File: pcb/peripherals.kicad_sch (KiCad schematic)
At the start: 32 parts, among them U2 PCA9545APW, U3 AHT20-F, U4 LTR-303ALS-01, U5 SGP40-D-R4

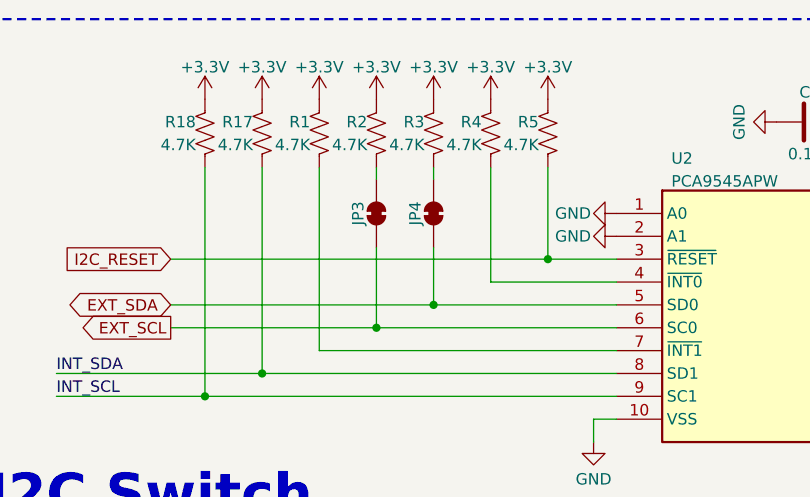
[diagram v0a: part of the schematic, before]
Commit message: Changed I2C to open instead of bridged
Moved I2C jumper to back
Changed to open instead of bridged
Changed Roxy to 5mm on front
Moved silkscreen around.
Updated renders
Removed logos from BOM
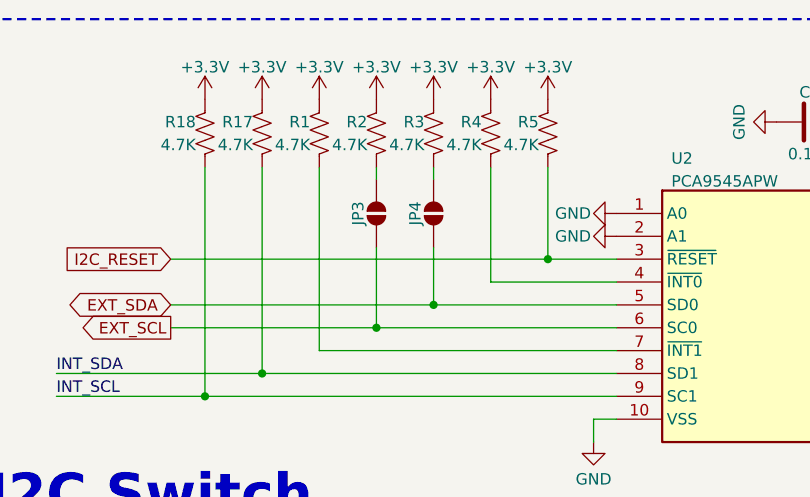
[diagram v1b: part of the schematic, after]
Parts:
- JP3, JP4: footprint CRGM Connector:SolderJumper-2_P1.3mm_Bridged_RoundedPad1.0x1.5mm -> CRGM Connector:SolderJumper-2_P1.3mm_Open_RoundedPad1.0x1.5mm; symbol Jumper:SolderJumper_2_Bridged -> CRGM Connector:SolderJumper_2_Open
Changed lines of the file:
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@@
 	)
 	(symbol
-		(lib_id "Jumper:SolderJumper_2_Bridged")
+		(lib_id "CRGM Connector:SolderJumper_2_Open")
 		(at 64.77 36.83 90)
 		(unit 1)
@@
 			)
 		)
-		(property "Footprint" "CRGM Connector:SolderJumper-2_P1.3mm_Bridged_RoundedPad1.0x1.5mm"
-			(at 64.77 36.83 0)
+		(property "Footprint" "CRGM Connector:SolderJumper-2_P1.3mm_Open_RoundedPad1.0x1.5mm"
+			(at 75.184 36.83 0)
 			(effects
 				(font
@@
 		)
 		(property "Datasheet" "~"
-			(at 64.77 36.83 0)
+			(at 72.898 36.83 0)
 			(effects
 				(font
@@
 			)
 		)
-		(property "Description" "Solder Jumper, 2-pole, closed/bridged"
-			(at 64.77 36.83 0)
+		(property "Description" "Solder Jumper, 2-pole, open"
+			(at 70.104 36.83 0)
 			(effects
 				(font
@@
 	)
 	(symbol
-		(lib_id "Jumper:SolderJumper_2_Bridged")
+		(lib_id "CRGM Connector:SolderJumper_2_Open")
 		(at 58.42 36.83 90)
 		(unit 1)
@@
 			)
 		)
-		(property "Footprint" "CRGM Connector:SolderJumper-2_P1.3mm_Bridged_RoundedPad1.0x1.5mm"
-			(at 58.42 36.83 0)
+		(property "Footprint" "CRGM Connector:SolderJumper-2_P1.3mm_Open_RoundedPad1.0x1.5mm"
+			(at 68.834 36.83 0)
 			(effects
 				(font
@@
 		)
 		(property "Datasheet" "~"
-			(at 58.42 36.83 0)
+			(at 66.548 36.83 0)
 			(effects
 				(font
@@
 			)
 		)
-		(property "Description" "Solder Jumper, 2-pole, closed/bridged"
-			(at 58.42 36.83 0)
+		(property "Description" "Solder Jumper, 2-pole, open"
+			(at 63.754 36.83 0)
 			(effects
 				(font

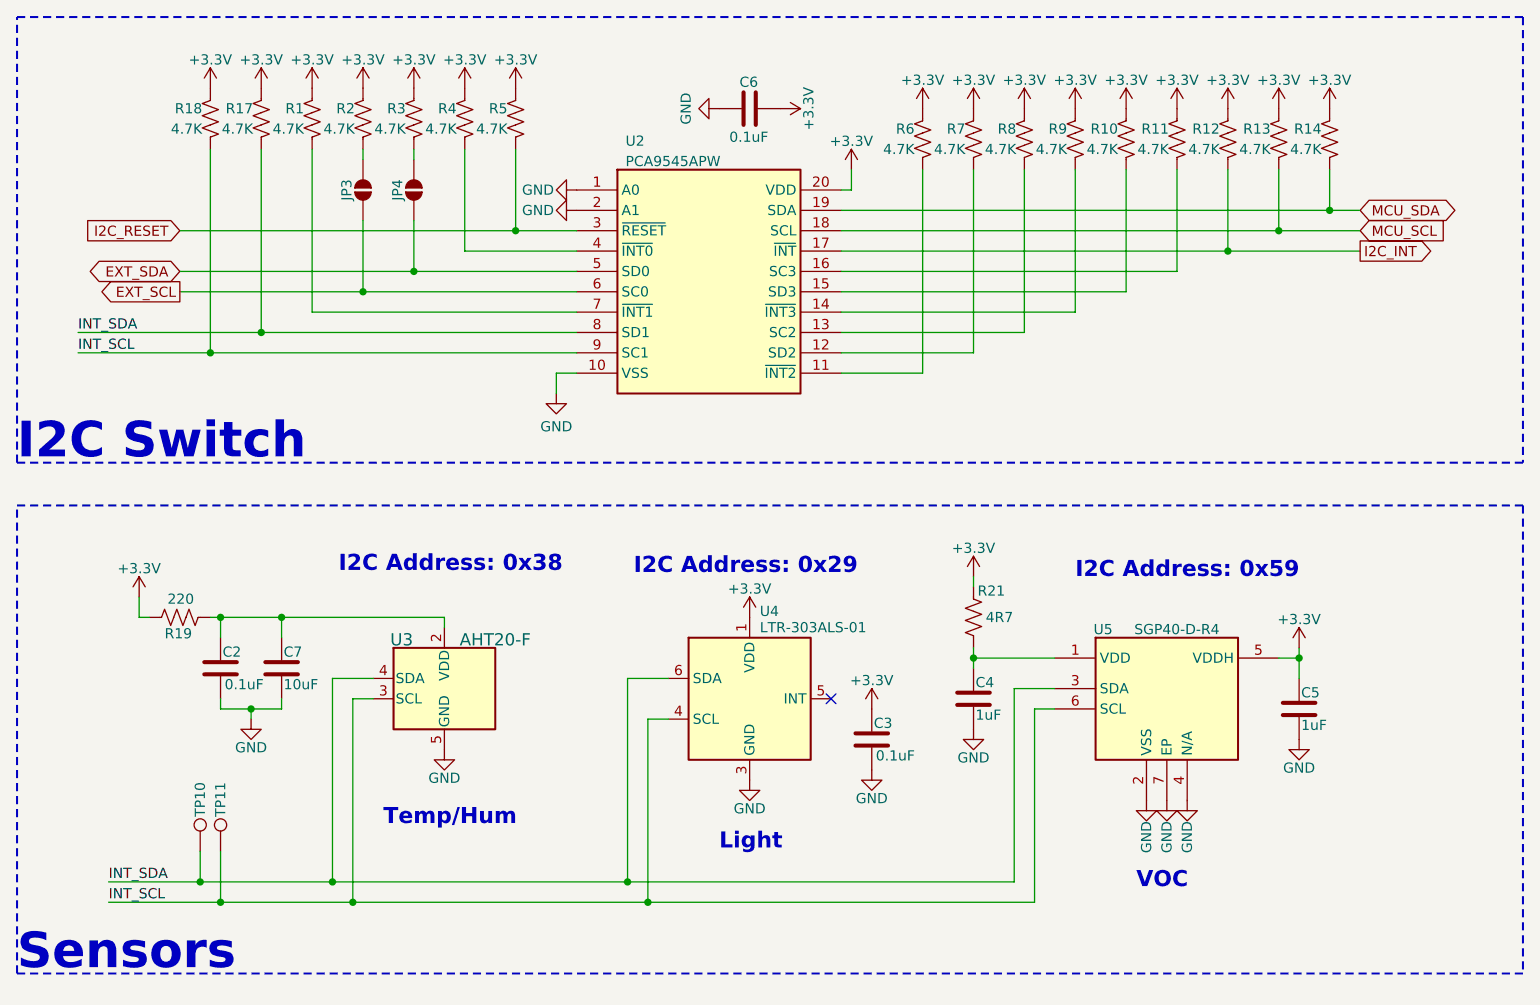
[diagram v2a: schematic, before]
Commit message: Redesign with cutouts for sensors
Removed power connectors since 5V is not needed
Added cutout for VOC sensor
Rerouted sensor section
Rescaled logos and fixed silkscreen
Changed to blue LED for power indicator
Updated requirements and renders
Changed all 0.1uF caps to small symbol
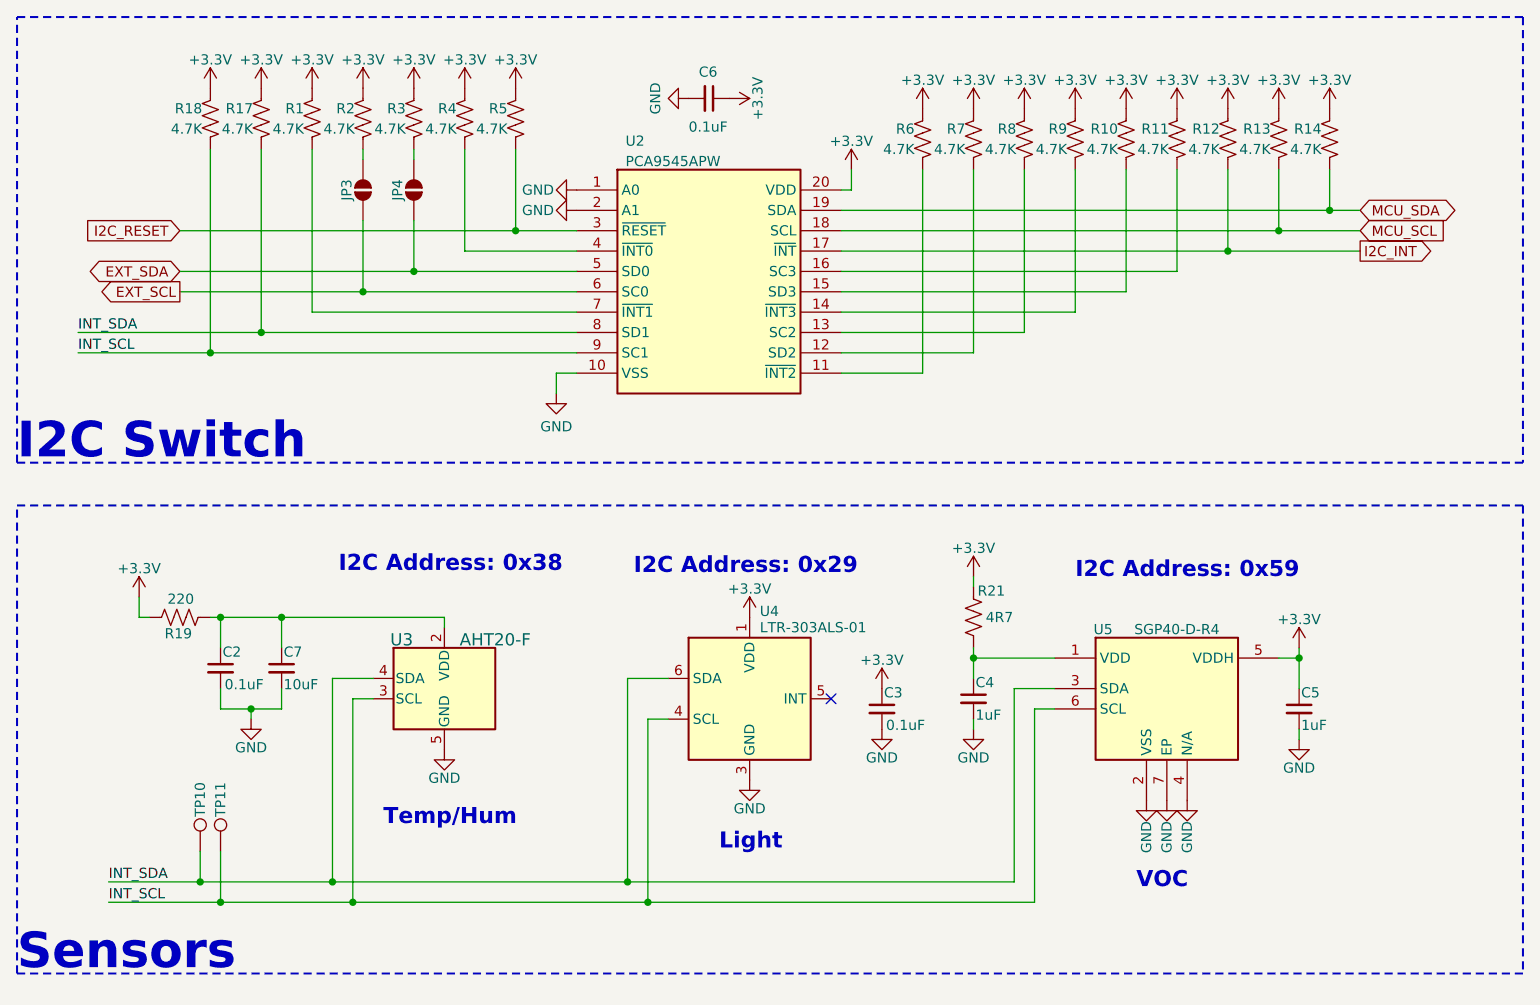
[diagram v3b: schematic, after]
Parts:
- C2, C3, C4, C5, C6, C7: symbol Device:C -> Device:C_Small
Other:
- moved on the sheet: C3, C6

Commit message: Updated UPDI Connector
Integrated serial and UPDI
Changed to vertical connectors
Updated renders
Rounded cutouts
Adjusted silkscreen
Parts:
- U2: LCSC C129515 -> C400709; LCSC_ALT (none) -> C129515
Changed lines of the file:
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@@
 			)
 		)
-		(property "LCSC" "C129515"
+		(property "LCSC" "C400709"
 			(at 101.6 79.248 0)
 			(effects
 				(font
+					(size 1.27 1.27)
+				)
+				(hide yes)
+			)
+		)
+		(property "LCSC_ALT" "C129515"
+			(at 101.6 48.26 0)
+			(effects
+				(font

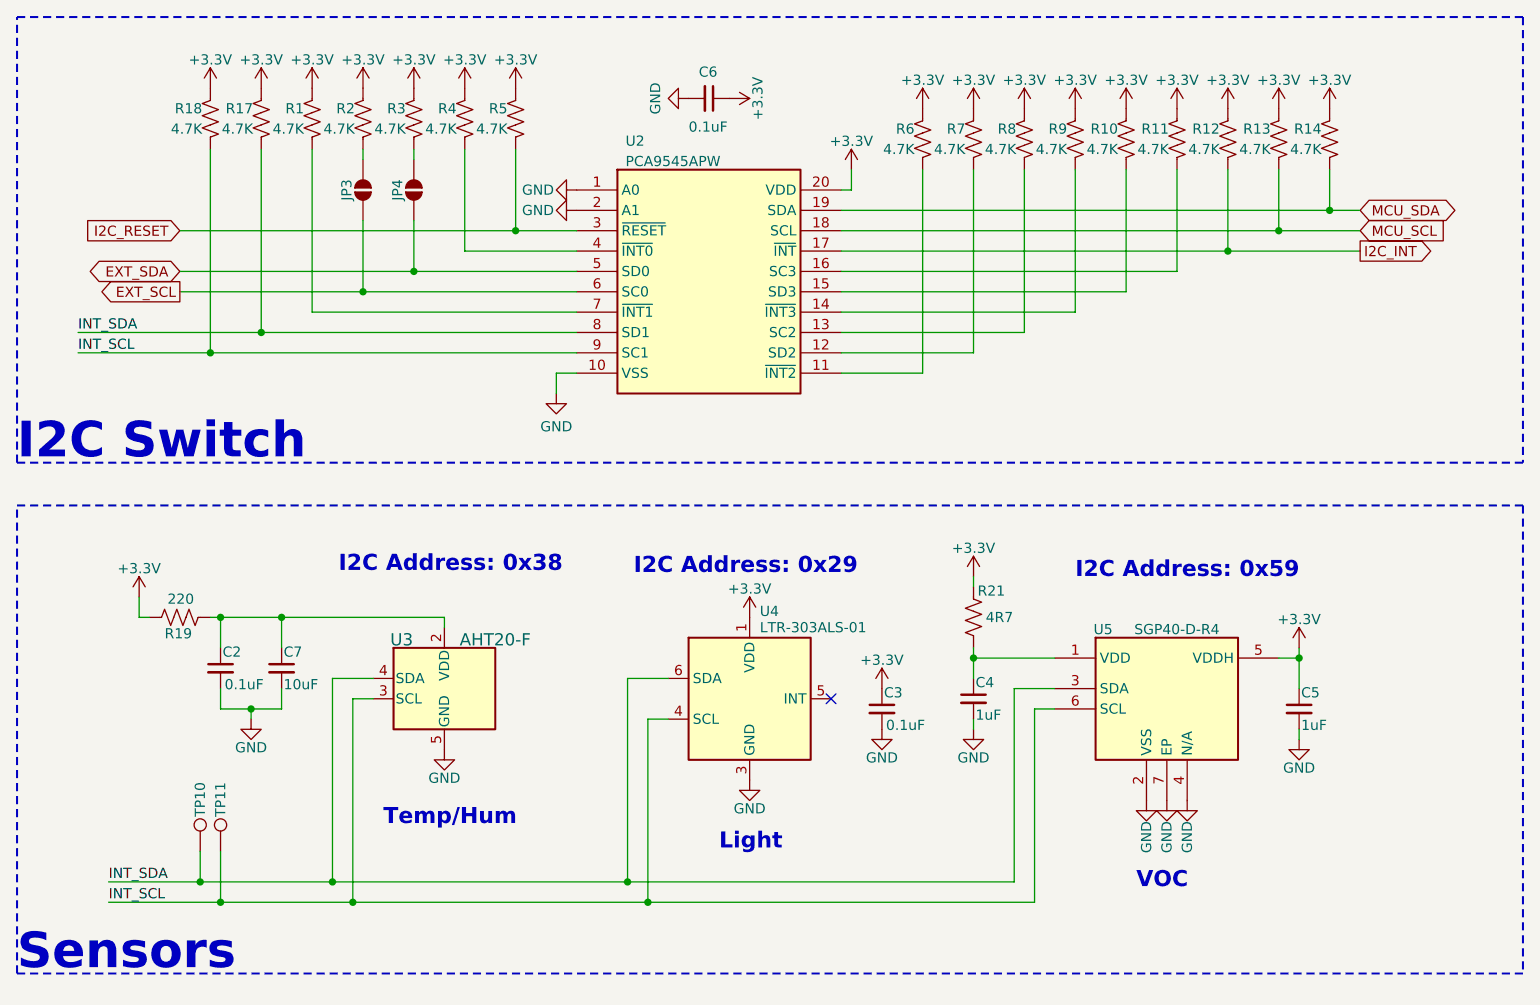
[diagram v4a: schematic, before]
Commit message: Changed to inside cutouts
Updated renders
Increased size of Roxy on front ❤️
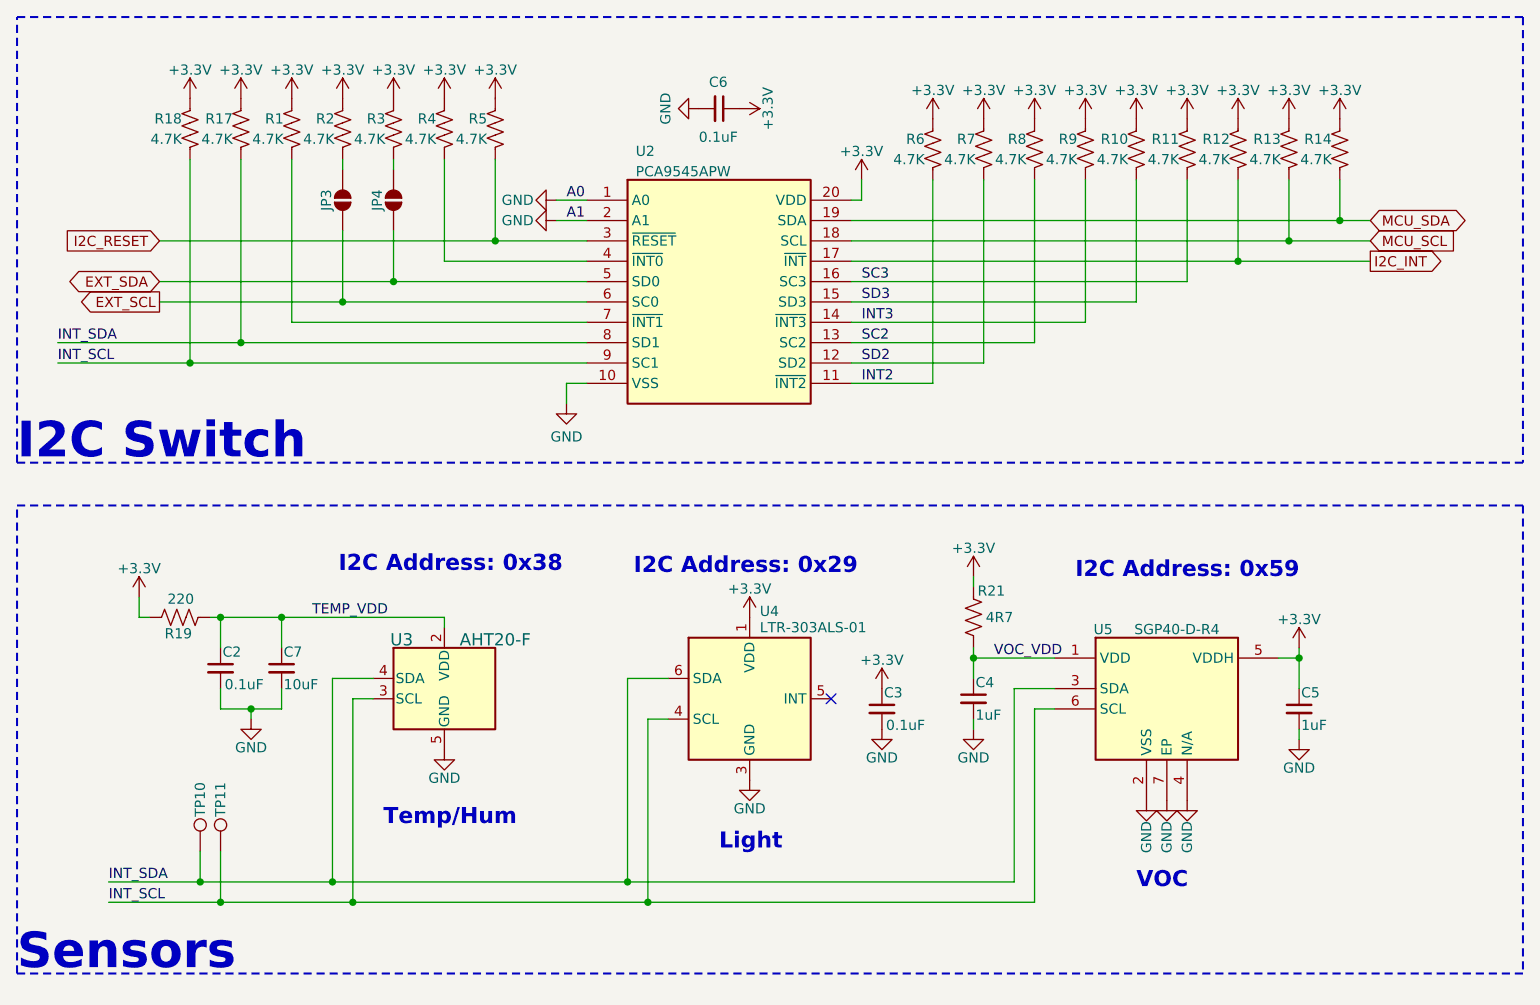
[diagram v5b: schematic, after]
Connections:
- net TEMP_VDD: now reaches C2.1, C7.1, R19.2, U3.2 (VDD)
- net INT3: now reaches R9.1, U2.14 (~{INT3})
- net VOC_VDD: now reaches C4.1, R21.2, U5.1 (VDD)
- net SD3: now reaches R10.1, U2.15 (SD3)
- net INT2: now reaches R6.1, U2.11 (~{INT2})
- net SC3: now reaches R11.1, U2.16 (SC3)
- net SD2: now reaches R7.1, U2.12 (SD2)
- net SC2: now reaches R8.1, U2.13 (SC2)
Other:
- moved on the sheet: C6, JP3, JP4, R1, R10, R11, R12, R13, R14, R17, R18, R2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

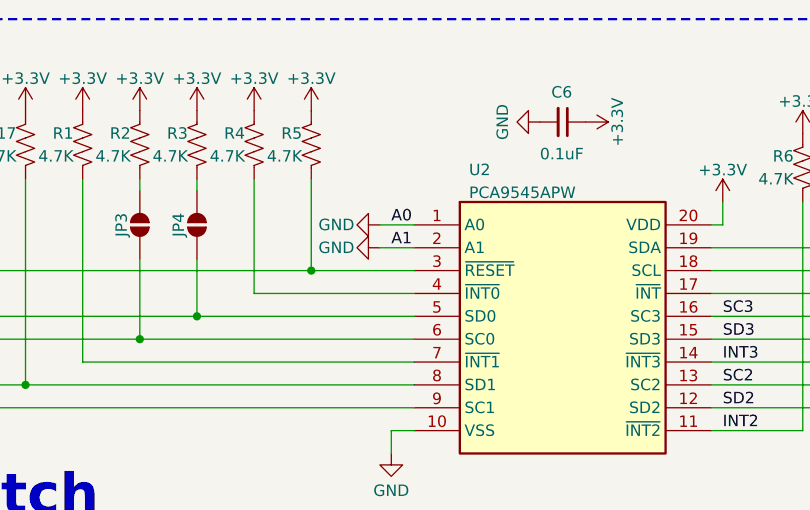
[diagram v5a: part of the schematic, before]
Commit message: Adjusted spacing and alignment of parts
Moved temp and voc to be on grid
Updated renders
Ran ERC -- fixed errors
Ran DRC -- fixed errors
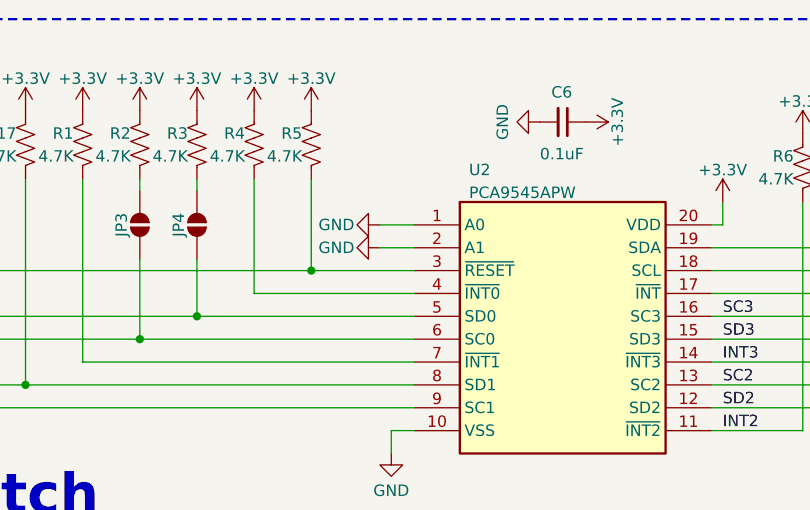
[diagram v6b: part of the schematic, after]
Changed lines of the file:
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@@
-		)
-	)
-	(label "A1"
-		(at 83.82 40.64 0)
-		(effects
-			(font
-				(size 1.27 1.27)
-			)
-			(justify left bottom)
-		)
-	)
-	(label "A0"
-		(at 83.82 38.1 0)
-		(effects
-			(font
-				(size 1.27 1.27)
-			)
-			(justify left bottom)
 		)
 	)
